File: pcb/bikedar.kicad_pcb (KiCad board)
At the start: 4 copper layers, 50 x 50 mm, 45 parts, among them IC1 ADP3335, IC2 BGT24MTR12, IC3 AD8541, IC4 AD8226, IC5 AD8226, IC6 AD8226, IC7 AD8226, IC8 AD8541, J1 CONN_02x10, X1 M3_MOUNT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

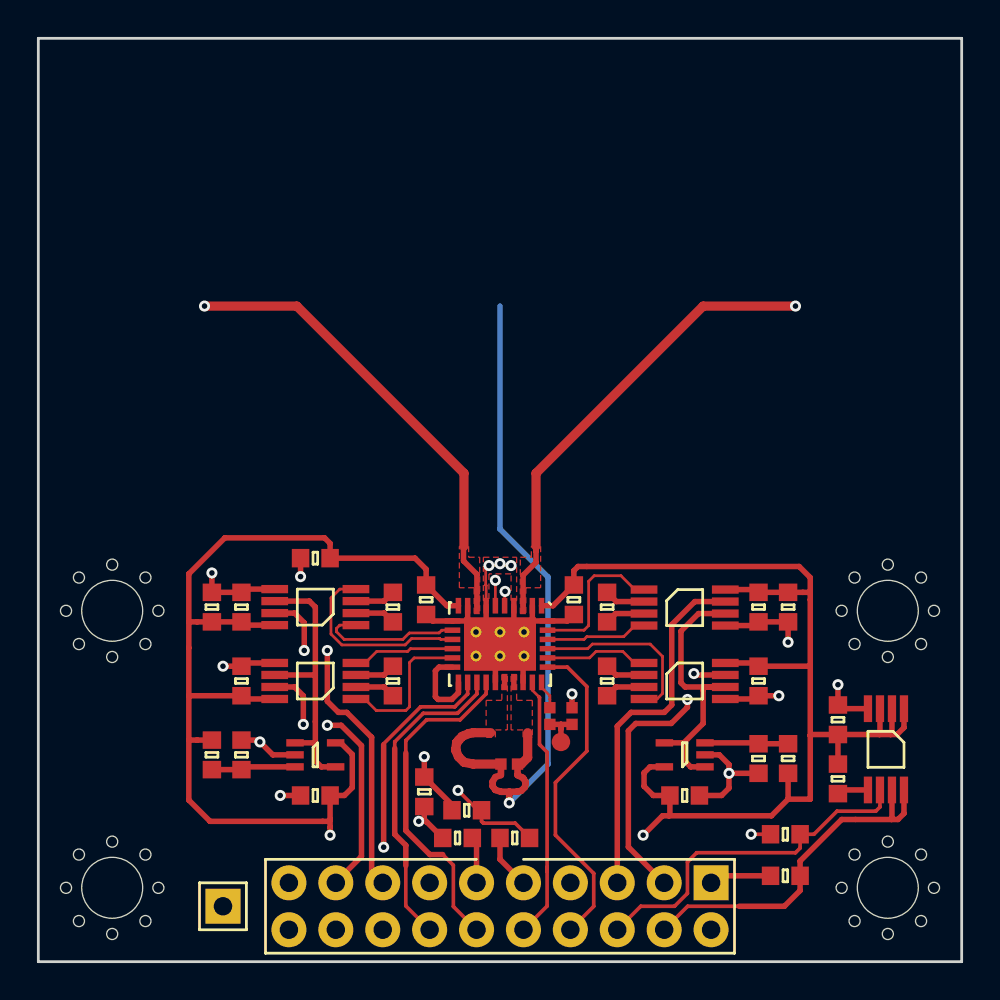
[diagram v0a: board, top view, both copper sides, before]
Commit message: tidy up and add lots of gnd
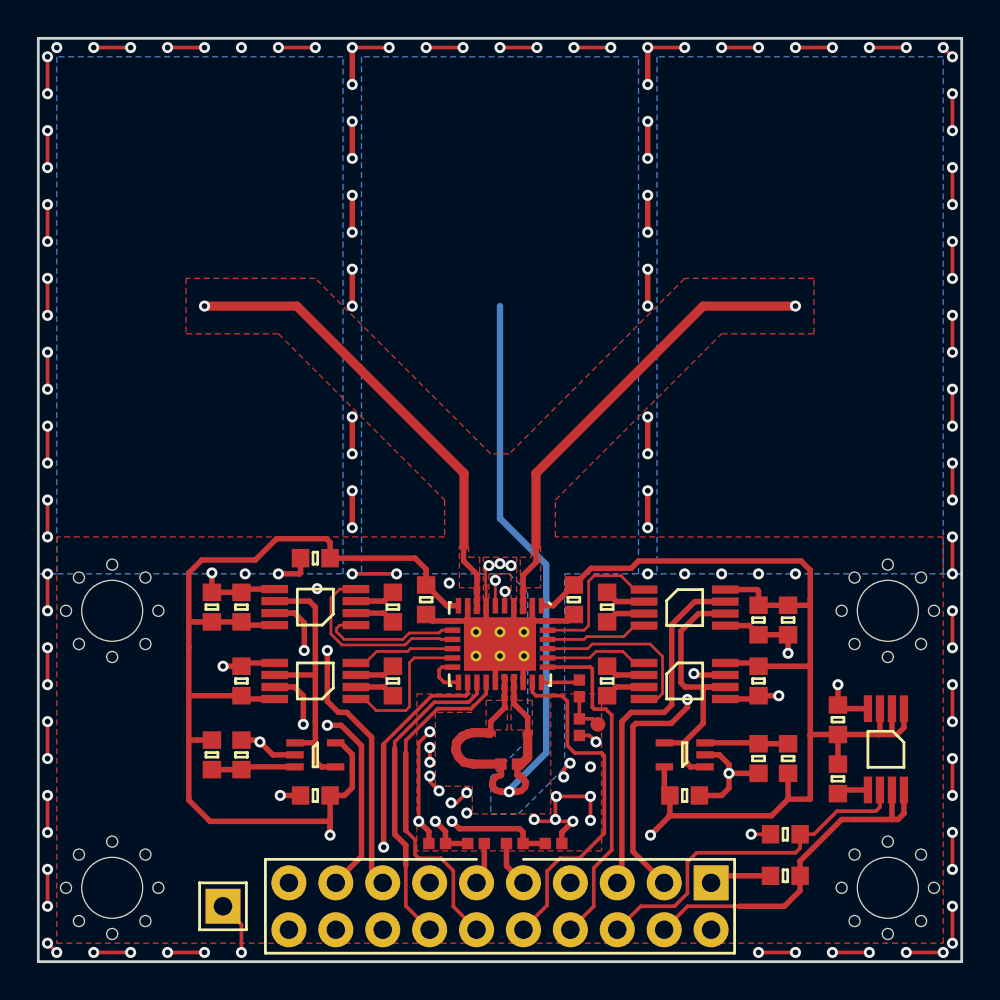
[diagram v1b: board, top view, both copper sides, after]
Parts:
- C5, C6, R1, R2: footprint agg:0603 -> agg:0402
- moved C5 5.03 mm to (77.9, 93.6), turned to 0 degrees
- moved C6 2.89 mm to (71.6, 93.6), turned to 0 degrees
- moved TP1 2.21 mm to (80.3, 87.2)
- moved C9 2.19 mm to (79.3, 85.2)
- moved R2 1.04 mm to (73.7, 93.6)
- moved R3 0.72 mm to (79.3, 87.3), turned to 90 degrees
- moved C11 0.70 mm to (89.0, 81.5)
- moved C15 0.70 mm to (90.6, 81.5)
- moved R1 0.30 mm to (75.8, 93.6)
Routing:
- net GND: track 66.2 -> 352.4 mm, vias 15 -> 151
- net /TX: track 41.9 -> 46.6 mm
- net /ANA: track 14.5 -> 19.1 mm
- net Net-(C5-Pad1): track 19.8 -> 23.0 mm
- net Net-(IC2-Pad16): track 4.43 -> 2.35 mm
- net 3v3: track 136.6 -> 135.5 mm
- net Net-(C6-Pad2): track 19.5 -> 20.3 mm
- net Net-(C9-Pad2): track 1.56 -> 2.38 mm
- added copper zone on B.Cu, net GND

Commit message: more rf work..
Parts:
- C5, C6: value 1µ -> 100n
- moved R13 0.81 mm to (76.0, 89.9)
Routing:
- net GND: track 352.4 -> 381.4 mm, vias 151 -> 150
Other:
- board text added: "Microstrips @ 24.125GHz 70.7R: 0.29mm wide, 90' = 1.96mm long 50R: 0.55mm wide, 180' = 3.79mm long"

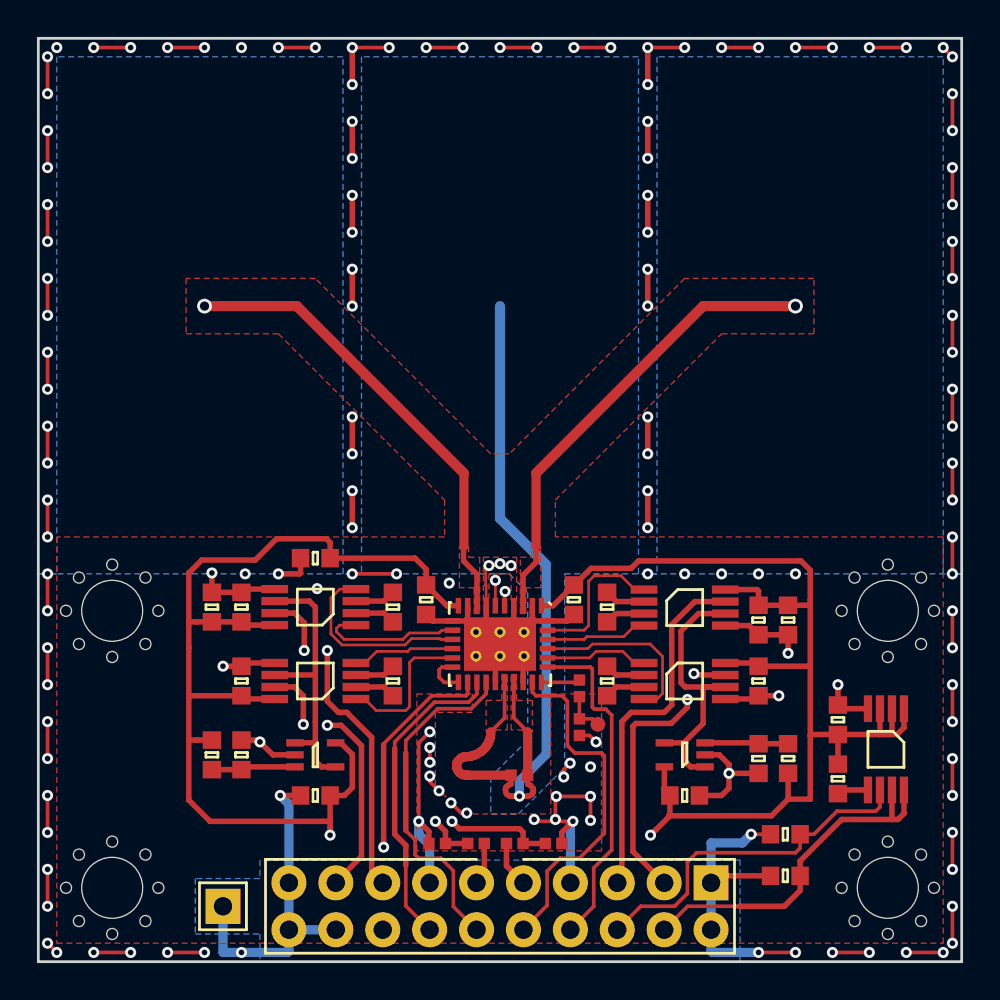
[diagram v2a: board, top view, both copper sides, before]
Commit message: nicer balun
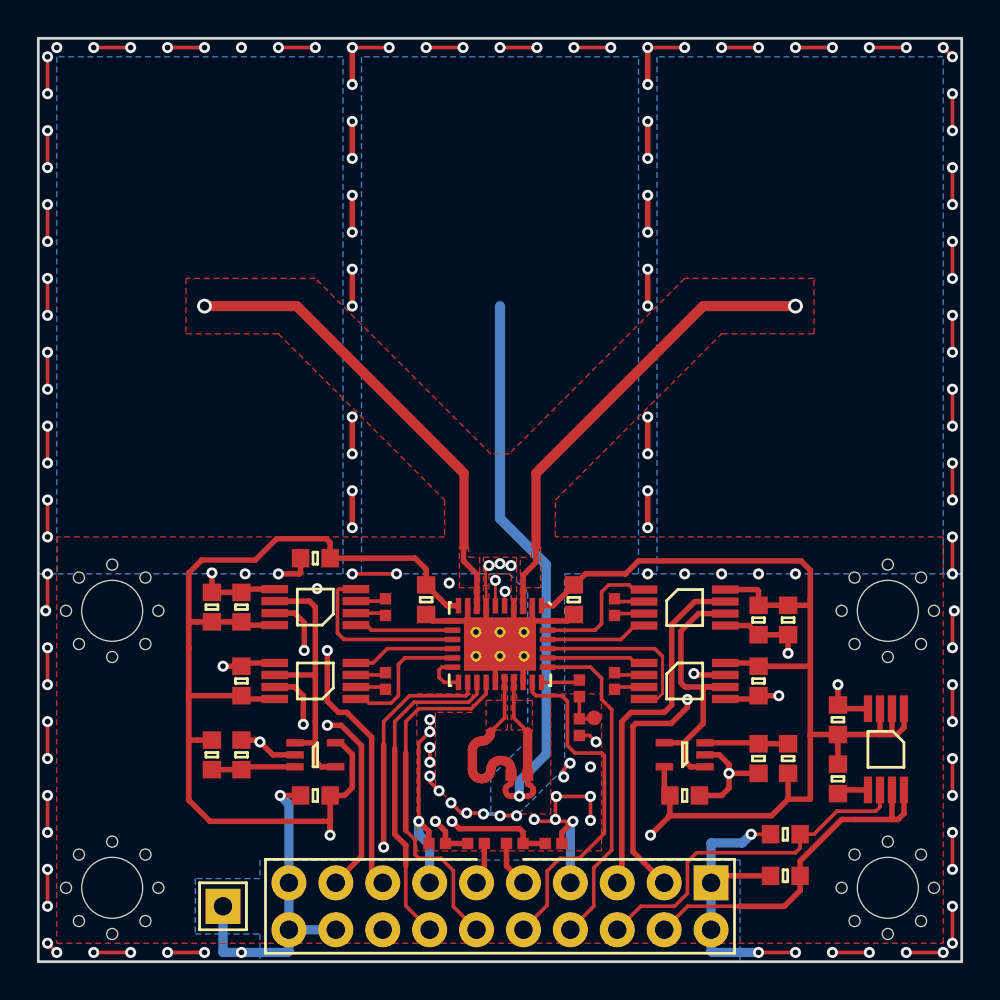
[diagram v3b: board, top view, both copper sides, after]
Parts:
- R6, R7, R8, R9: footprint agg:0603 -> agg:0402
- moved TP1 0.40 mm to (80.1, 86.8)
- moved R6 0.40 mm to (81.2, 84.8)
- moved R7 0.40 mm to (81.2, 80.8)
- moved R8 0.40 mm to (68.8, 84.8)
- moved R9 0.40 mm to (68.8, 80.8)
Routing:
- net GND: track 381.4 -> 385.0 mm, vias 150 -> 154
- net /IFQ2_N: track 7.97 -> 5.34 mm
- net /IFI2_N: track 8.57 -> 7.33 mm
- net /IFQ2_P: track 10.5 -> 9.70 mm
- net /~CS: track 17.4 -> 18.1 mm
- net /CLK: track 17.1 -> 17.7 mm
- net /SI: track 18.6 -> 19.2 mm
- net Net-(IC7-Pad3): track 2.20 -> 1.65 mm
- net Net-(IC7-Pad2): track 2.20 -> 1.65 mm
- net Net-(IC6-Pad3): track 2.20 -> 1.65 mm
- net Net-(IC6-Pad2): track 2.20 -> 1.65 mm
- net Net-(IC4-Pad3): track 2.20 -> 1.65 mm
- net Net-(IC4-Pad2): track 2.20 -> 1.65 mm
- net Net-(IC5-Pad3): track 2.19 -> 1.64 mm
- net Net-(IC5-Pad2): track 2.21 -> 1.66 mm

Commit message: further tidying
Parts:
- moved R3 1.30 mm to (79.3, 86.0), turned to 0 degrees
- moved R10 1.18 mm to (89.5, 93.8)
- moved C1 0.96 mm to (89.5, 95.5)
- moved C9 0.40 mm to (79.3, 84.8), turned to 180 degrees
- moved TP1 0.11 mm to (80.2, 86.8)
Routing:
- net 3v3: track 135.5 -> 145.5 mm
- net GND: track 385.0 -> 388.6 mm, vias 154 -> 160
- net /TX: track 46.5 -> 47.6 mm
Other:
- board text added: "Microstrips @ 24.125GHz on Ro3450 (εr=3.66) 70.7R: 0.28mm wide, 90' = 1.93mm long 50R: 0.54mm wide, 180' = 3.71mm long"
- board text removed: "Microstrips @ 24.125GHz 70.7R: 0.29mm wide, 90' = 1.96mm long 50R: 0.55mm wide, 180' = 3.79mm long"

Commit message: further tidying
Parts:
- added C18: 1µ, agg:0603, F.Cu at (79.8, 77.8)
- moved C8 5.22 mm to (70.2, 77.8)
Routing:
- net 3v3: track 145.5 -> 148.2 mm
- net GND: track 388.6 -> 390.3 mm

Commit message: further tidying
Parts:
- added C19: 10µ, agg:0603, F.Cu at (90.6, 84.8)
- added C20: 10µ, agg:0603, F.Cu at (59.4, 84.8)
- added D1: LED, agg:0603-LED, F.Cu at (98.2, 90.2)
- added R14: 1k, agg:0603, F.Cu at (98.2, 86.8)
- moved C11 0.70 mm to (89.0, 80.8)
- moved C15 0.70 mm to (90.6, 80.8)
- moved IC1 0.30 mm to (95.6, 88.5)
- moved C2 0.30 mm to (93.0, 90.1)
- moved C3 0.30 mm to (93.0, 86.9)
- moved C5 0.30 mm to (78.2, 93.6)
- moved R1 0.30 mm to (76.1, 93.6)
- moved C6 0.20 mm to (71.8, 93.6)
- moved R2 0.20 mm to (73.9, 93.6)
- moved R4 0.20 mm to (90.6, 88.8)
- moved R5 0.20 mm to (89.0, 88.8)
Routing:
- net 3v3: track 148.2 -> 141.0 mm
- net GND: track 390.3 -> 394.7 mm, vias 160 -> 161
- net /VREF2: track 15.2 -> 18.9 mm, vias 0 -> 4
- net Net-(D1-Pad2): track 0.00 -> 1.70 mm
- net /IFQ2: track 18.7 -> 17.6 mm, vias 2 -> 0
- net /IFI2: track 14.9 -> 14.0 mm, vias 2 -> 0
- net /COARSE: track 2.30 -> 2.98 mm

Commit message: further tidying
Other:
- board text added: "AG r1"
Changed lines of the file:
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@@
     (area 49.649999 49.749999 158.157143 101.5325)
     (thickness 1)
-    (drawings 126)
+    (drawings 127)
     (tracks 907)
     (zones 0)
@@
     (1 In1.Cu signal hide)
     (2 In2.Cu signal hide)
-    (31 B.Cu signal hide)
+    (31 B.Cu signal)
     (32 B.Adhes user)
     (33 F.Adhes user)
@@
     )
   )
+  (gr_text "AG\nr1" (at 53 88.2) (layer F.Cu)
+    (effects (font (size 1.5 1.5) (thickness 0.3)))
+  )
   (gr_line (start 76 65) (end 76 65) (layer Dwgs.User) (width 0.1))
   (gr_line (start 74 69) (end 74 65) (layer Dwgs.User) (width 0.1))
@@
       )
     )
+  )
+  (zone (net 0) (net_name "") (layer F.Mask) (hatch edge 0.508)
+    (connect_pads (clearance 0))
+    (min_thickness 0.254)
+    (fill yes (arc_segments 16) (thermal_gap 0.508) (thermal_bridge_width 0.508))
+    (polygon
+      (pts
+        (xy 50.5 85.5) (xy 55 85.5) (xy 55 91) (xy 50.5 91)
+      )
+    )

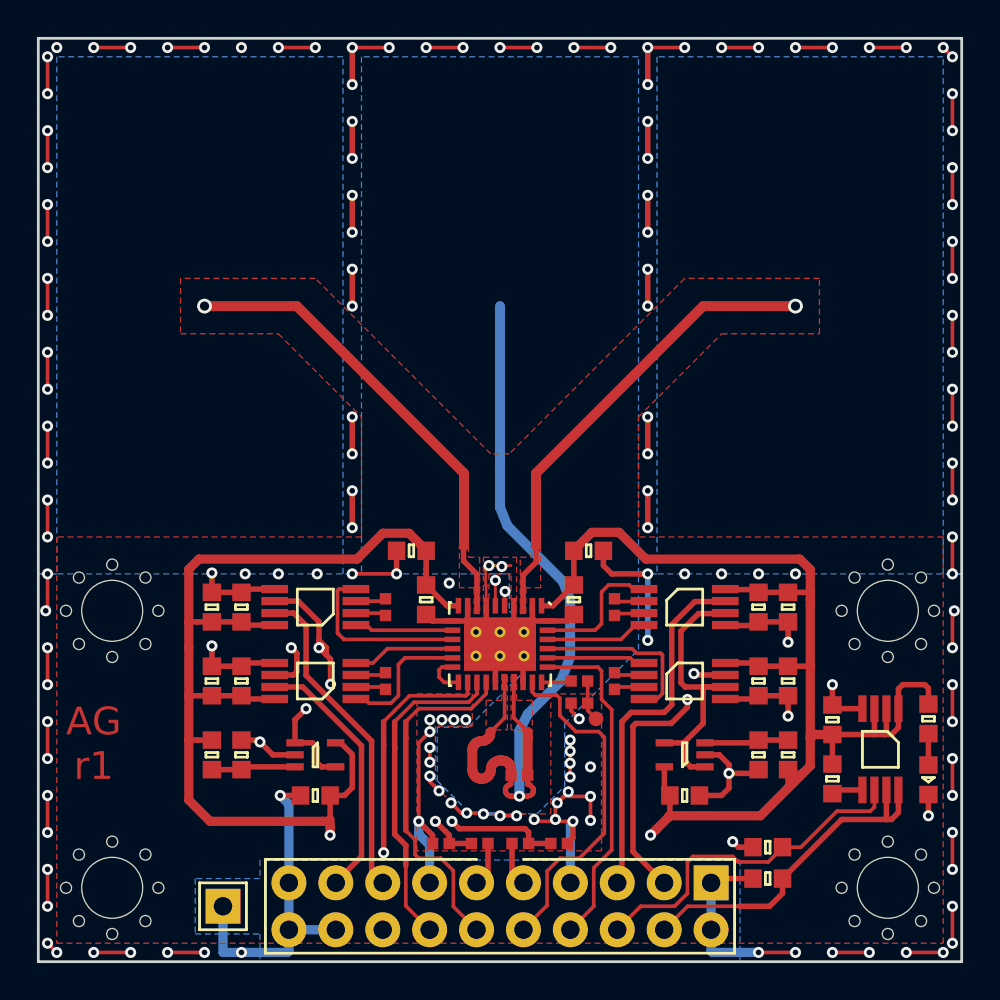
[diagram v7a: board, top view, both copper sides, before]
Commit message: final tidying. almost ready to go but vias wrong size?!
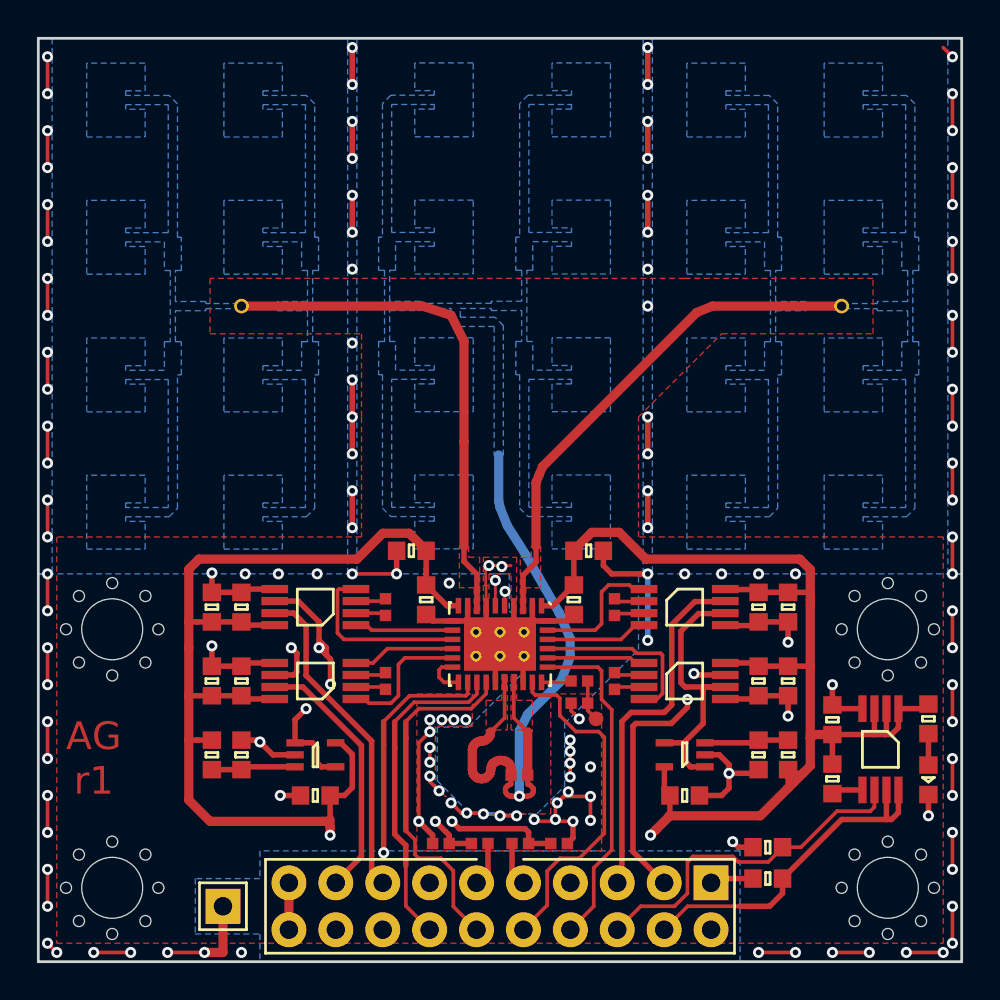
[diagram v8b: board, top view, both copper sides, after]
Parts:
- added AE2: , X0, B.Cu at (93.5, 64.5)
- added AE3: , X0, B.Cu at (61.0, 64.5)
- moved X3 1.00 mm to (96.0, 82.0)
- moved X4 1.00 mm to (54.0, 82.0)
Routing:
- net GND: track 394.7 -> 329.7 mm, vias 161 -> 139
- net /TX: track 47.2 -> 38.8 mm
- net /RX2: track 25.6 -> 27.6 mm, vias 1 -> 0
- net /RX1: track 25.6 -> 27.6 mm, vias 1 -> 0
- net 3v3: track 141.0 -> 139.0 mm
- added copper zone on B.Cu, net /RX1
- added copper zone on B.Cu, net /RX2
- added copper zone on B.Cu, net /TX
